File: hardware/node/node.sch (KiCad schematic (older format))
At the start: 58 parts, among them J1 BOOT0_Jumper, J2 FTDI, J3 SMA Female, J5 SWD, Q1 Si2323DDS, SW1 TVCM04N016BB, U1 RFM69HCW, U2 SHTC3, U3 AT25DF512C, U4 STM32L031K6Tx, Y1 32.768K-CFPX217

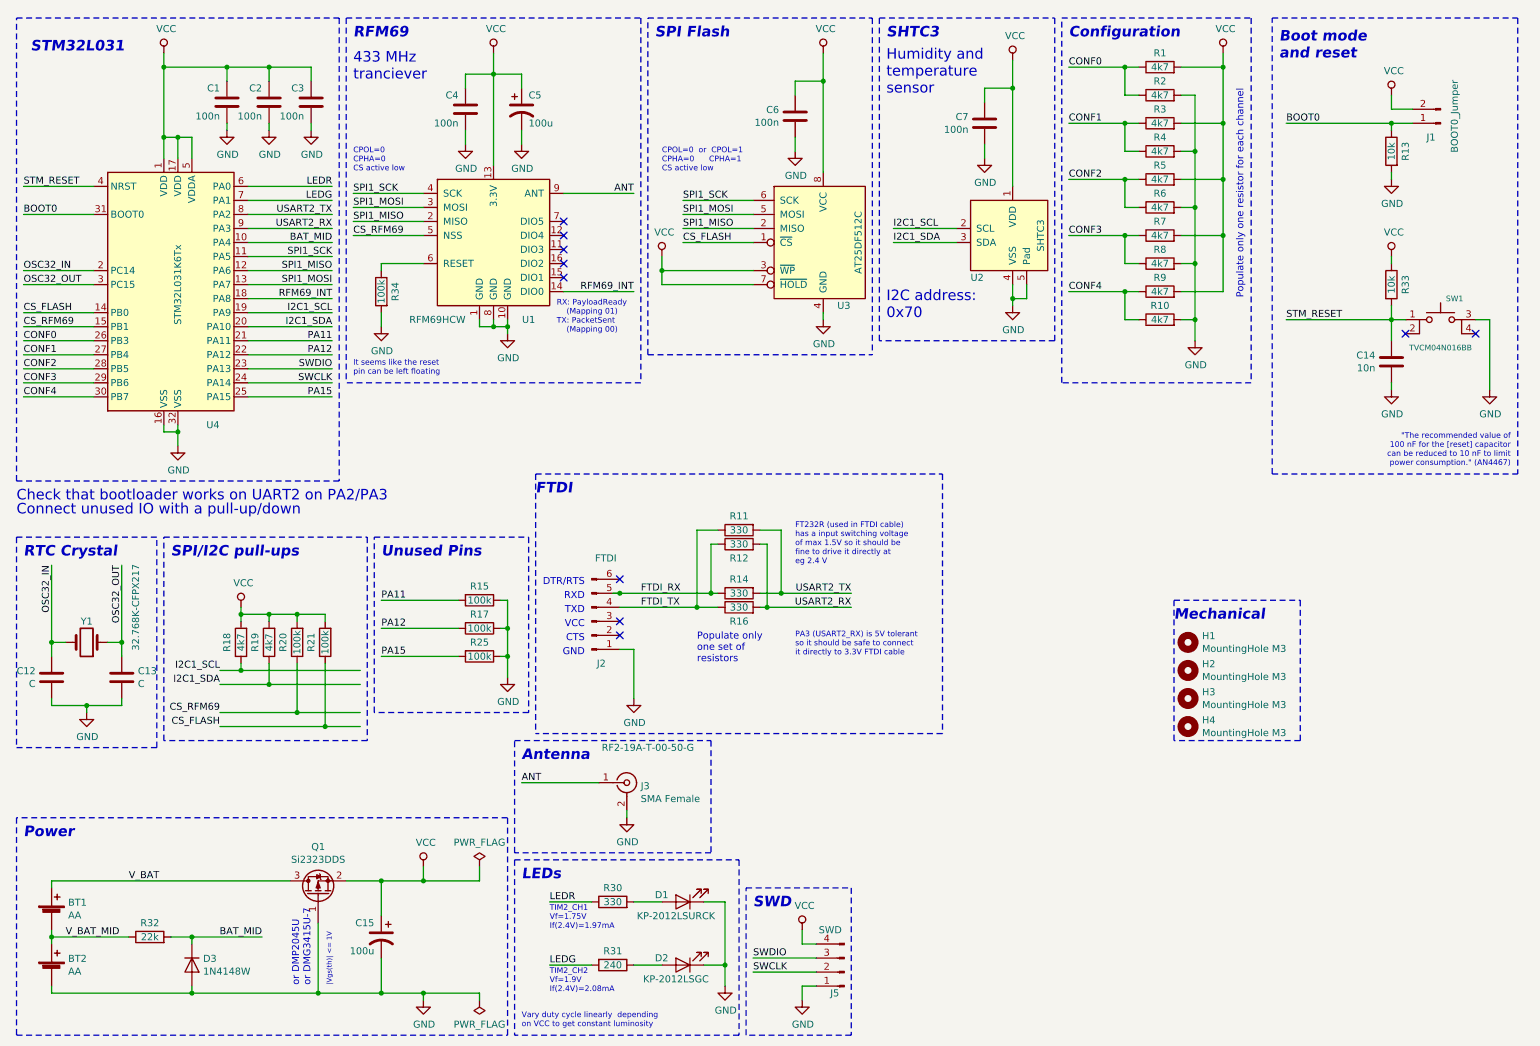
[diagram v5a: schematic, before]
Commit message: PCB with batteries on JST PH
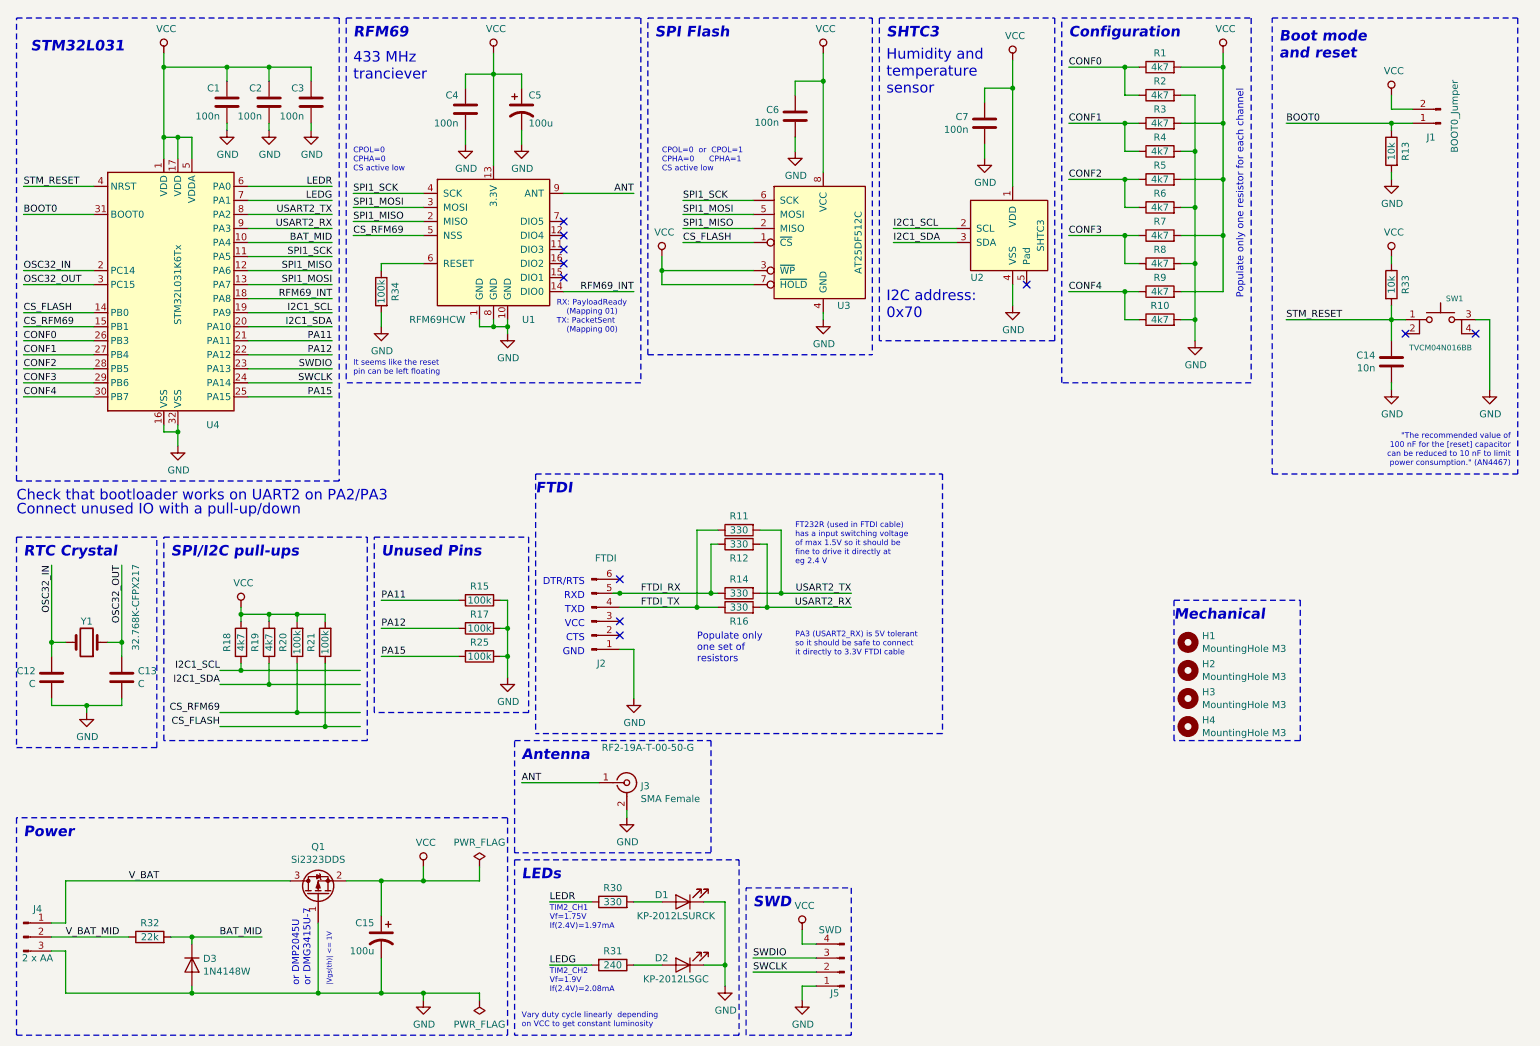
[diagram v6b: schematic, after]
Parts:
- removed BT1, BT2: AA, humidity:AA_Battery_Holder, symbol Device:Battery_Cell
- added J4: 2 x AA, Connector_JST:JST_PH_S3B-PH-K_1x03_P2.00mm_Horizontal, symbol Connector:Conn_01x03_Male
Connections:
- net GND: now also J4.3 (Pin_3); no longer U2.5 (Pad)
- net V_BAT: now also J4.1 (Pin_1)
- net V_BAT_MID: now also J4.2 (Pin_2)
- no-connect marks 10 -> 11
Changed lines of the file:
@@
 $EndComp
-Wire Wire Line
-	7600 2400 7600 2500
-Wire Wire Line
-	7600 2500 7700 2500
-Wire Wire Line
-	7700 2500 7700 2400
-Connection ~ 7600 2500
-Wire Wire Line
-	7600 2500 7600 2550
 Wire Wire Line
 	10400 2650 10300 2650
@@
 Wire Notes Line
 	8750 5650 8750 4650
-$Comp
-L Device:Battery_Cell BT1
-U 1 1 5E042F5F
-P 750 6900
-F 0 "BT1" H 868 6996 50  0000 L CNN
-F 1 "AA" H 868 6905 50  0000 L CNN
-F 2 "humidity:AA_Battery_Holder" V 750 6960 50  0001 C CNN
-F 3 "https://www.electrokit.com/produkt/batterihallare-1xaa-pcb/" V 750 6960 50  0001 C CNN
-F 4 "electrokit: 41003559" H 750 6900 50  0001 C CNN "Part"
-	1    750  6900
-	1    0    0    -1
-$EndComp
-Wire Wire Line
-	750  6650 750  6700
-Wire Wire Line
-	750  6650 2450 6650
-Wire Wire Line
-	750  7100 750  7050
+Wire Wire Line
+	850  6650 2450 6650
 Wire Wire Line
 	750  7050 1300 7050
-Connection ~ 750  7050
-Wire Wire Line
-	750  7050 750  7000
-Wire Wire Line
-	750  7450 750  7400
-Wire Wire Line
-	750  7450 1750 7450
-$Comp
-L Device:Battery_Cell BT2
-U 1 1 5E0BA08E
-P 750 7300
-F 0 "BT2" H 868 7396 50  0000 L CNN
-F 1 "AA" H 868 7305 50  0000 L CNN
-F 2 "humidity:AA_Battery_Holder" V 750 7360 50  0001 C CNN
-F 3 "https://www.electrokit.com/produkt/batterihallare-1xaa-pcb/" V 750 7360 50  0001 C CNN
-F 4 "electrokit: 41003559" H 750 7300 50  0001 C CNN "Part"
-	1    750  7300
-	1    0    0    -1
-$EndComp
+Wire Wire Line
+	850  7450 1750 7450
 Text Label 850  7050 0    50   ~ 0
 V_BAT_MID
@@
 Wire Wire Line
 	4800 4600 5450 4600
+$Comp
+L Connector:Conn_01x03_Male J4
+U 1 1 5CEF0263
+P 550 7050
+F 0 "J4" H 650 7250 50  0000 C CNN
+F 1 "2 x AA" H 650 6900 50  0000 C CNN
+F 2 "Connector_JST:JST_PH_S3B-PH-K_1x03_P2.00mm_Horizontal" H 550 7050 50  0001 C CNN
+F 3 "~" H 550 7050 50  0001 C CNN
+	1    550  7050
+	1    0    0    -1
+$EndComp
+Wire Wire Line
+	850  6650 850  6950
+Wire Wire Line
+	850  6950 750  6950
+Wire Wire Line
+	850  7450 850  7150
+Wire Wire Line
+	850  7150 750  7150
+Wire Wire Line
+	7600 2400 7600 2550
+NoConn ~ 7700 2400
 $EndSCHEMATC

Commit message: Battery connector on the other side
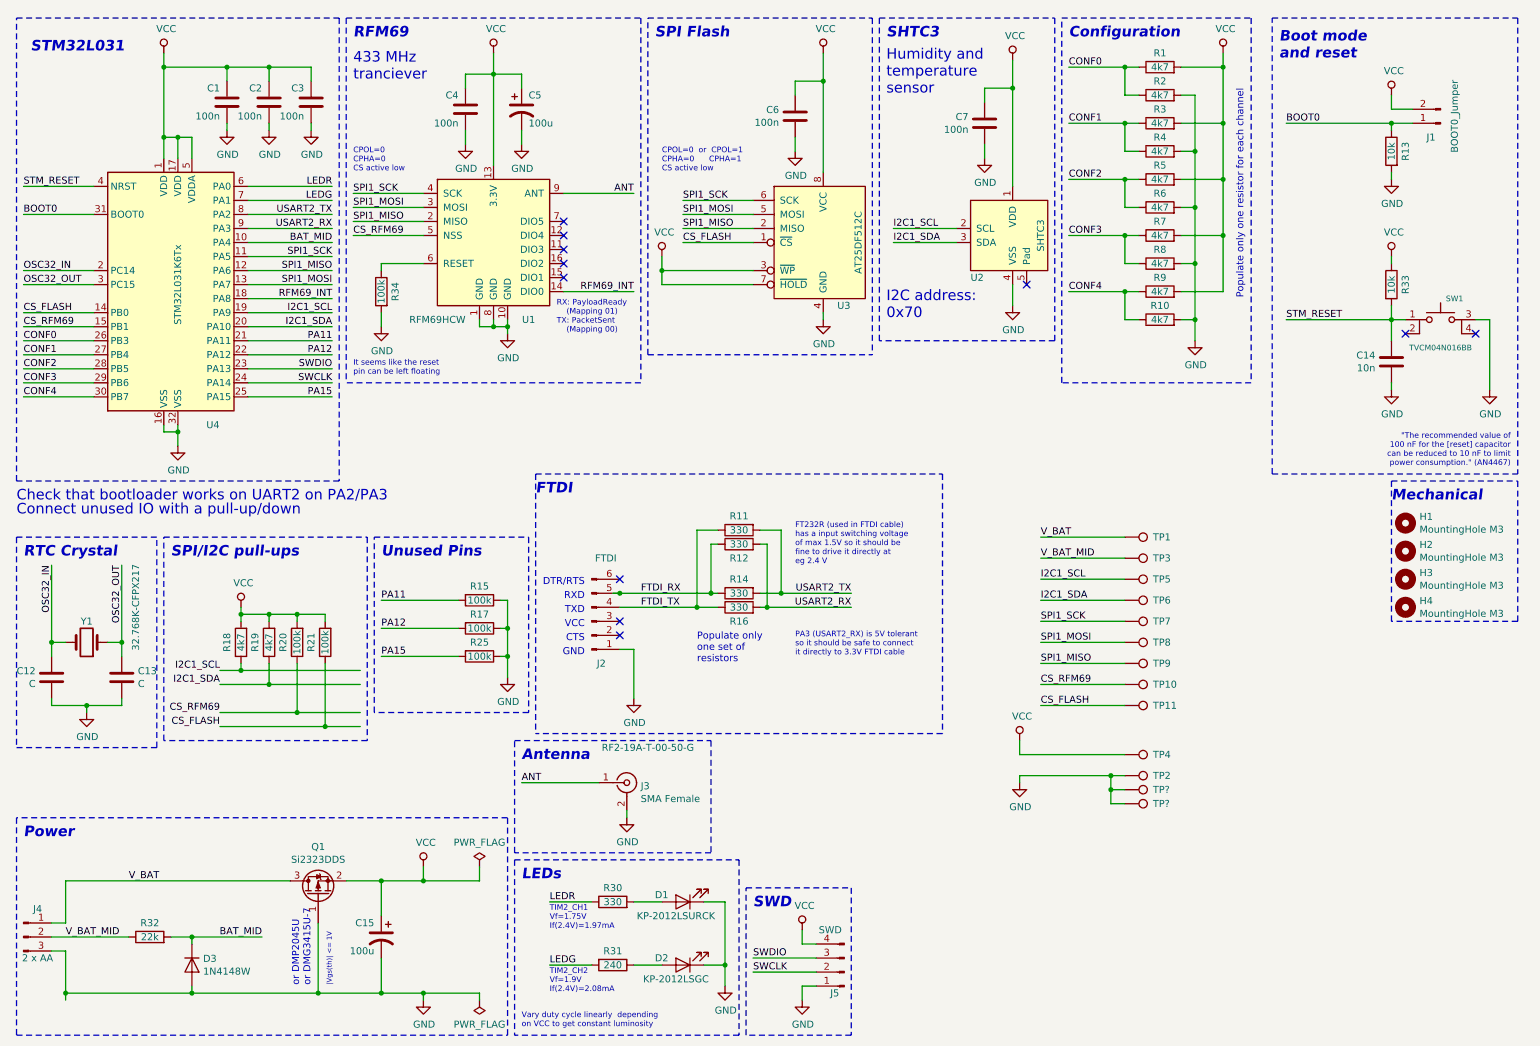
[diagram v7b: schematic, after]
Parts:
- added TP1, TP10, TP11, TP2, TP3, TP4, TP5, TP6, TP7, TP8, TP9, TP? (x2): TestPoint, TestPoint:TestPoint_THTPad_D1.5mm_Drill0.7mm, symbol Connector:TestPoint
- J1: footprint Connector_PinHeader_2.54mm:PinHeader_1x02_P2.54mm_Horizontal -> Connector_PinHeader_2.54mm:PinHeader_1x02_P2.54mm_Vertical
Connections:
- net CS_FLASH: now also TP11.1
- net CS_RFM69: now also TP10.1
- net GND: now also TP2.1, TP?.1, TP?.1
- net I2C1_SCL: now also TP5.1
- net I2C1_SDA: now also TP6.1
- net SPI1_MISO: now also TP9.1
- net SPI1_MOSI: now also TP8.1
- net SPI1_SCK: now also TP7.1
- net VCC: now also TP4.1
- net V_BAT: now also TP1.1
- net V_BAT_MID: now also TP3.1
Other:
- moved on the sheet: H1, H2, H3, H4

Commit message: Connect RFM69 reset to STM32
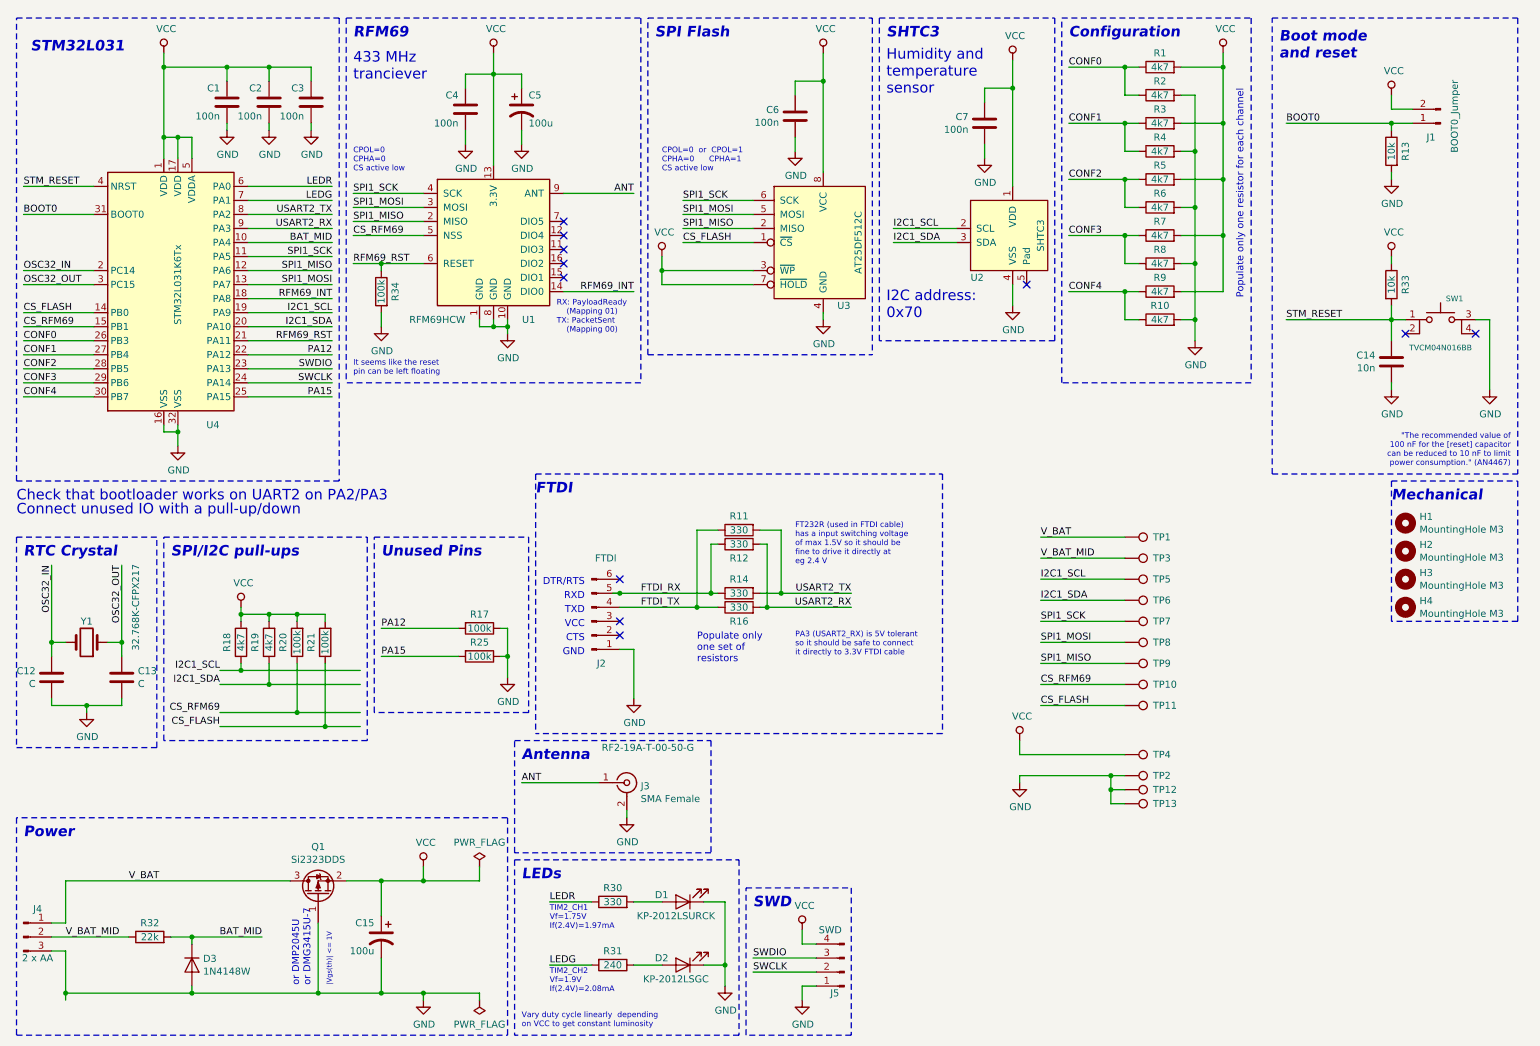
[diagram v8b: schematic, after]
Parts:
- removed R15: 100k, Resistor_SMD:R_0603_1608Metric_Pad1.05x0.95mm_HandSolder, symbol Device:R
- TP12, TP13: renamed from TP?; footprint TestPoint:TestPoint_THTPad_D1.5mm_Drill0.7mm -> TestPoint:TestPoint_THTPad_1.5x1.5mm_Drill0.7mm
- TP2: footprint TestPoint:TestPoint_THTPad_D1.5mm_Drill0.7mm -> TestPoint:TestPoint_THTPad_1.5x1.5mm_Drill0.7mm
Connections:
- net PA11 is gone; now on net RFM69_RST: U4.21 (PA11)
- net RFM69_RST: now reaches R34.1, U1.6 (RESET)
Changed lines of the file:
@@
 Wire Wire Line
 	2150 2700 2750 2700
-Text Label 2750 2700 2    50   ~ 0
-I2C1_SDA
 Wire Wire Line
 	2150 2900 2750 2900
@@
 Text Label 2750 2900 2    50   ~ 0
 PA12
-Text Label 3100 4650 0    50   ~ 0
-PA11
-Text Label 2750 2800 2    50   ~ 0
-PA11
 Text Label 3100 4850 0    50   ~ 0
 PA12
@@
 	0    1    1    0
 $EndComp
-$Comp
-L Device:R R15
-U 1 1 5D5F1930
-P 3800 4650
-F 0 "R15" V 3700 4650 50  0000 C CNN
-F 1 "100k" V 3800 4650 50  0000 C CNN
-F 2 "Resistor_SMD:R_0603_1608Metric_Pad1.05x0.95mm_HandSolder" V 3730 4650 50  0001 C CNN
-F 3 "~" H 3800 4650 50  0001 C CNN
-	1    3800 4650
-	0    1    1    0
-$EndComp
-Wire Wire Line
-	3100 4650 3650 4650
 Wire Wire Line
 	3650 4850 3100 4850
-Wire Wire Line
-	3950 4650 4000 4650
-Wire Wire Line
-	4000 4650 4000 4850
 Connection ~ 4000 5050
 Wire Wire Line
 	3950 4850 4000 4850
-Connection ~ 4000 4850
 Wire Wire Line
 	4000 4850 4000 5050
@@
 F 0 "TP2" V 8400 6100 50  0000 L CNN
 F 1 "TestPoint" H 8458 5929 50  0001 L CNN
-F 2 "TestPoint:TestPoint_THTPad_D1.5mm_Drill0.7mm" H 8600 5900 50  0001 C CNN
+F 2 "TestPoint:TestPoint_THTPad_1.5x1.5mm_Drill0.7mm" H 8600 5900 50  0001 C CNN
 F 3 "~" H 8600 5900 50  0001 C CNN
 	1    8400 5900
@@
 	7800 5250 8400 5250
 $Comp
-L Connector:TestPoint TP?
+L Connector:TestPoint TP12
 U 1 1 5D229E6E
 P 8400 6000
-F 0 "TP?" V 8400 6200 50  0000 L CNN
+F 0 "TP12" V 8400 6200 50  0000 L CNN
 F 1 "TestPoint" H 8458 6029 50  0001 L CNN
-F 2 "TestPoint:TestPoint_THTPad_D1.5mm_Drill0.7mm" H 8600 6000 50  0001 C CNN
+F 2 "TestPoint:TestPoint_THTPad_1.5x1.5mm_Drill0.7mm" H 8600 6000 50  0001 C CNN
 F 3 "~" H 8600 6000 50  0001 C CNN
 	1    8400 6000
@@
 $EndComp
 $Comp
-L Connector:TestPoint TP?
+L Connector:TestPoint TP13
 U 1 1 5D229F08
 P 8400 6100
-F 0 "TP?" V 8400 6300 50  0000 L CNN
+F 0 "TP13" V 8400 6300 50  0000 L CNN
 F 1 "TestPoint" H 8458 6129 50  0001 L CNN
-F 2 "TestPoint:TestPoint_THTPad_D1.5mm_Drill0.7mm" H 8600 6100 50  0001 C CNN
+F 2 "TestPoint:TestPoint_THTPad_1.5x1.5mm_Drill0.7mm" H 8600 6100 50  0001 C CNN
 F 3 "~" H 8600 6100 50  0001 C CNN
 	1    8400 6100
@@
 	8300 6100 8400 6100
 Connection ~ 8300 6000
+Text Label 2900 2250 0    50   ~ 0
+RFM69_RST
+Wire Wire Line
+	3100 2250 2900 2250
+Connection ~ 3100 2250
+Text Label 2750 2700 2    50   ~ 0
+I2C1_SDA
+Text Label 2750 2800 2    50   ~ 0
+RFM69_RST
 $EndSCHEMATC
